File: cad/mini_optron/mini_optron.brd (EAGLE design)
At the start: 67 x 39.4 mm, 10 parts

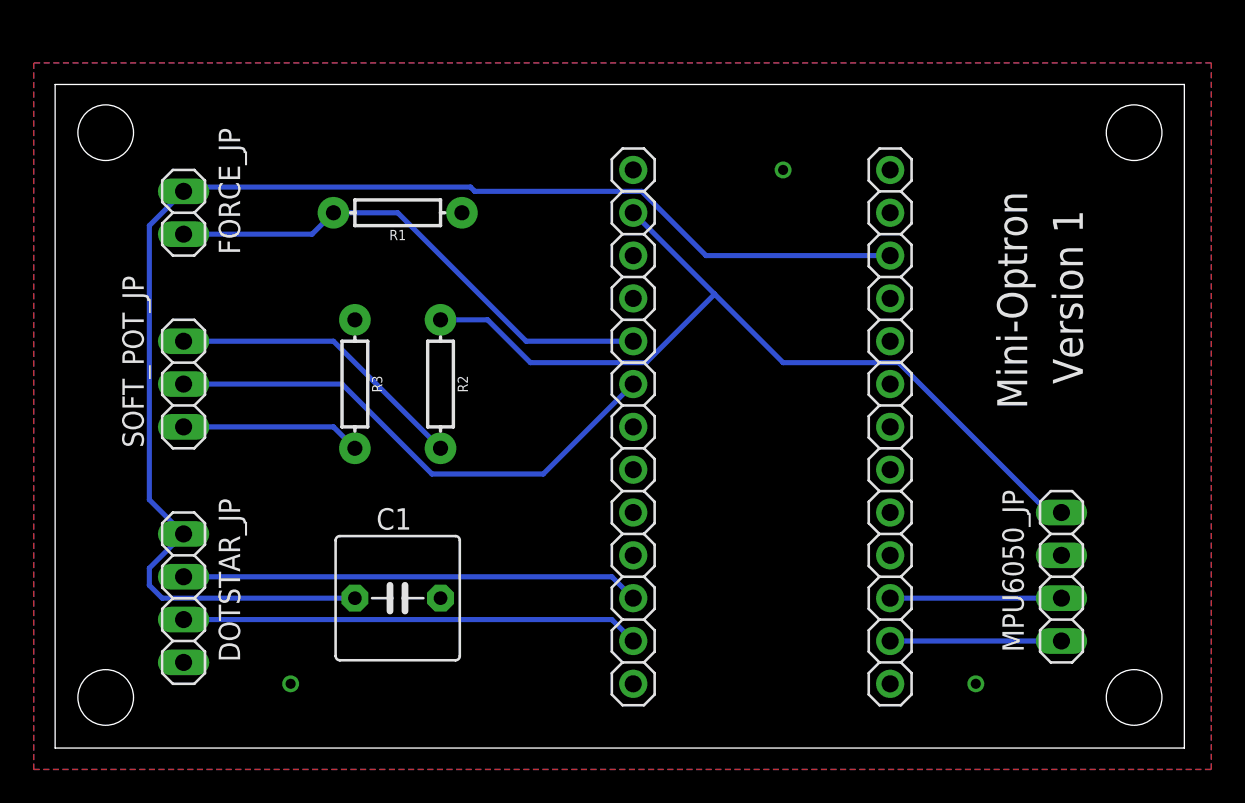
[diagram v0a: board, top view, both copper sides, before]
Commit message: Updated FSR circuit, c1 orient
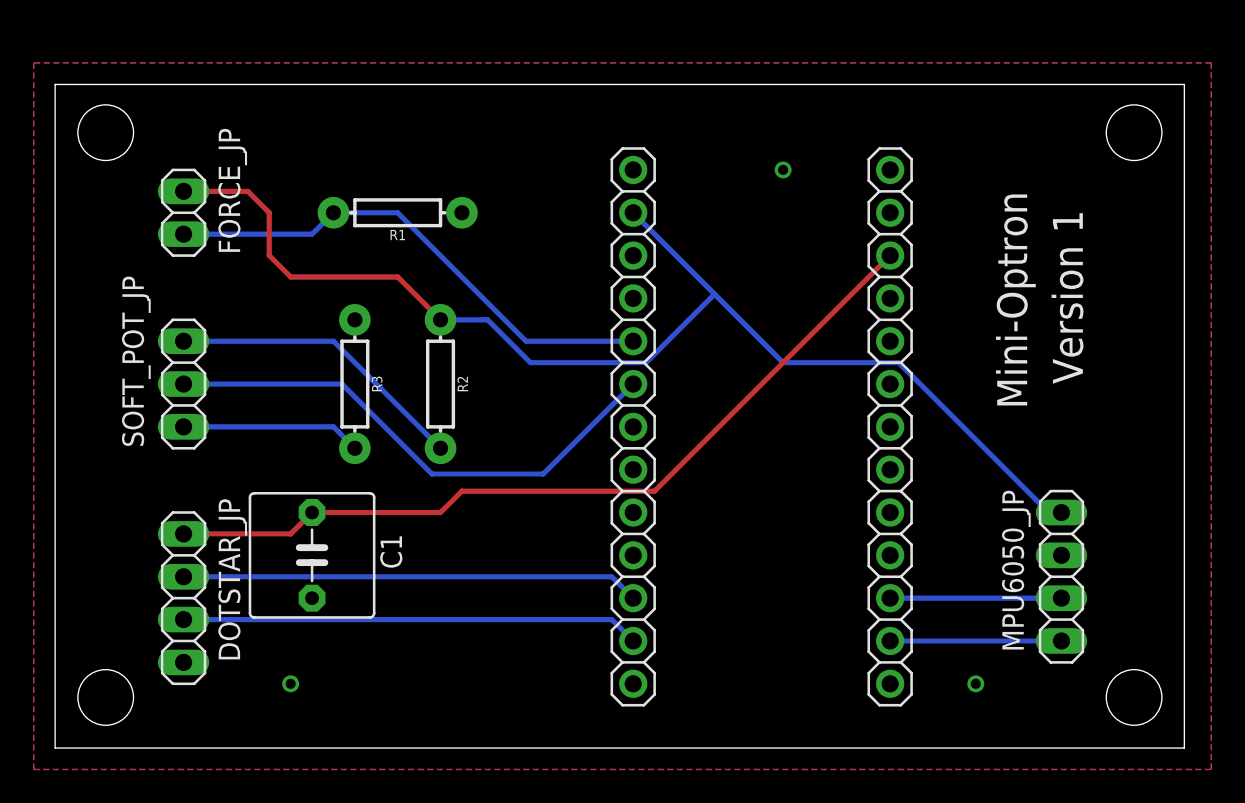
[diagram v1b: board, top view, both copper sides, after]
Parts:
- R1: value 2.2k -> 33k
- moved C1 5.68 mm to (15.2, 11.4), turned to 270 degrees
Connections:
- net CONN: now also FORCE_JP.1
- net VCC: no longer FORCE_JP.1
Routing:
- net VCC: track 82.1 -> 48.7 mm
- net CONN: track 51.8 -> 71.6 mm
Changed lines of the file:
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@@
 <?xml version="1.0" encoding="utf-8"?>
 <!DOCTYPE eagle SYSTEM "eagle.dtd">
-<eagle version="9.6.1">
+<eagle version="9.3.1">
 <drawing>
 <settings>
@@
 </autorouter>
 <elements>
-<element name="C1" library="capacitor-wima" library_urn="urn:adsk.eagle:library:116" package="C5B7.2" package3d_urn="urn:adsk.eagle:package:5430/1" value="1 uF" x="20.32" y="8.89" smashed="yes">
-<attribute name="MF" value="AVX" x="36.83" y="5.08" size="1.778" layer="27" display="off"/>
-<attribute name="MPN" value="0805YD105KAT2A" x="36.83" y="5.08" size="1.778" layer="27" display="off"/>
-<attribute name="NAME" x="19.05" y="12.954" size="1.27" layer="25" ratio="10"/>
-<attribute name="OC_NEWARK" value="95W9236" x="36.83" y="5.08" size="1.778" layer="27" display="off"/>
-<attribute name="POPULARITY" value="1" x="36.83" y="5.08" size="1.778" layer="27" display="off"/>
-<attribute name="VALUE" x="18.415" y="3.429" size="1.27" layer="27" ratio="10"/>
+<element name="C1" library="capacitor-wima" library_urn="urn:adsk.eagle:library:116" package="C5B7.2" package3d_urn="urn:adsk.eagle:package:5430/1" value="1 uF" x="15.24" y="11.43" smashed="yes" rot="R270">
+<attribute name="MF" value="AVX" x="11.43" y="-5.08" size="1.778" layer="27" rot="R270" display="off"/>
+<attribute name="MPN" value="0805YD105KAT2A" x="11.43" y="-5.08" size="1.778" layer="27" rot="R270" display="off"/>
+<attribute name="NAME" x="19.304" y="12.7" size="1.27" layer="25" ratio="10" rot="R270"/>
+<attribute name="OC_NEWARK" value="95W9236" x="11.43" y="-5.08" size="1.778" layer="27" rot="R270" display="off"/>
+<attribute name="POPULARITY" value="1" x="11.43" y="-5.08" size="1.778" layer="27" rot="R270" display="off"/>
+<attribute name="VALUE" x="9.779" y="13.335" size="1.27" layer="27" ratio="10" rot="R270"/>
 </element>
 <element name="DOTSTAR_JP" library="pinhead" library_urn="urn:adsk.eagle:library:325" package="1X04" package3d_urn="urn:adsk.eagle:package:22407/2" value="" x="7.62" y="8.89" smashed="yes" rot="R270">
@@
 <attribute name="VALUE" x="4.445" y="25.4" size="1.27" layer="27" rot="R270"/>
 </element>
-<element name="R1" library="SparkFun-Resistors" library_urn="urn:adsk.eagle:library:532" package="AXIAL-0.3" package3d_urn="urn:adsk.eagle:package:39658/1" value=" 2.2k" x="20.32" y="31.75" smashed="yes" rot="R180">
+<element name="R1" library="SparkFun-Resistors" library_urn="urn:adsk.eagle:library:532" package="AXIAL-0.3" package3d_urn="urn:adsk.eagle:package:39658/1" value="33k" x="20.32" y="31.75" smashed="yes" rot="R180">
 <attribute name="MF" value="VISHAY" x="20.32" y="31.75" size="1.778" layer="27" rot="R180" display="off"/>
 <attribute name="MPN" value="CRCW060310K0FKEA" x="20.32" y="31.75" size="1.778" layer="27" rot="R180" display="off"/>
@@
 <contactref element="C1" pad="1"/>
 <contactref element="DOTSTAR_JP" pad="1"/>
-<contactref element="FORCE_JP" pad="1"/>
-<wire x1="5.588" y1="10.668" x2="7.62" y2="12.7" width="0.3048" layer="16"/>
-<wire x1="5.588" y1="9.652" x2="5.588" y2="10.668" width="0.3048" layer="16"/>
-<wire x1="6.35" y1="8.89" x2="5.588" y2="9.652" width="0.3048" layer="16"/>
-<wire x1="17.78" y1="8.89" x2="6.35" y2="8.89" width="0.3048" layer="16"/>
-<wire x1="5.588" y1="30.988" x2="7.62" y2="33.02" width="0.3048" layer="16"/>
-<wire x1="5.588" y1="14.732" x2="5.588" y2="30.988" width="0.3048" layer="16"/>
-<wire x1="7.62" y1="12.7" x2="5.588" y2="14.732" width="0.3048" layer="16"/>
-<wire x1="38.608" y1="29.21" x2="49.53" y2="29.21" width="0.3048" layer="16"/>
-<wire x1="34.798" y1="33.02" x2="38.608" y2="29.21" width="0.3048" layer="16"/>
-<wire x1="24.892" y1="33.02" x2="34.798" y2="33.02" width="0.3048" layer="16"/>
-<wire x1="24.638" y1="33.274" x2="24.892" y2="33.02" width="0.3048" layer="16"/>
-<wire x1="7.874" y1="33.274" x2="24.638" y2="33.274" width="0.3048" layer="16"/>
-<wire x1="7.62" y1="33.02" x2="7.874" y2="33.274" width="0.3048" layer="16"/>
+<wire x1="49.53" y1="29.21" x2="35.56" y2="15.24" width="0.3048" layer="1"/>
+<wire x1="24.13" y1="15.24" x2="22.86" y2="13.97" width="0.3048" layer="1"/>
+<wire x1="22.86" y1="13.97" x2="15.24" y2="13.97" width="0.3048" layer="1"/>
+<wire x1="35.56" y1="15.24" x2="24.13" y2="15.24" width="0.3048" layer="1"/>
+<wire x1="15.24" y1="13.97" x2="13.97" y2="12.7" width="0.3048" layer="1"/>
+<wire x1="13.97" y1="12.7" x2="7.62" y2="12.7" width="0.3048" layer="1"/>
 </signal>
 <signal name="N$4">
@@
 <wire x1="35.052" y1="22.86" x2="28.194" y2="22.86" width="0.3048" layer="16"/>
 <wire x1="39.116" y1="26.924" x2="35.052" y2="22.86" width="0.3048" layer="16"/>
+<contactref element="FORCE_JP" pad="1"/>
+<wire x1="22.86" y1="25.4" x2="20.32" y2="27.94" width="0.3048" layer="1"/>
+<wire x1="13.97" y1="27.94" x2="12.7" y2="29.21" width="0.3048" layer="1"/>
+<wire x1="12.7" y1="29.21" x2="12.7" y2="31.75" width="0.3048" layer="1"/>
+<wire x1="12.7" y1="31.75" x2="11.43" y2="33.02" width="0.3048" layer="1"/>
+<wire x1="11.43" y1="33.02" x2="7.62" y2="33.02" width="0.3048" layer="1"/>
+<wire x1="20.32" y1="27.94" x2="13.97" y2="27.94" width="0.3048" layer="1"/>
 </signal>
 <signal name="N$2">

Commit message: Add files via upload
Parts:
- removed R2: 10k, SparkFun-Resistors:AXIAL-0.3
- R1: value 33k -> 10K
- moved MPU6050_JP 51.1 mm to (8.62, 11.9)
- moved DOTSTAR_JP 39.8 mm to (39.1, 33.2)
- moved C1 27.4 mm to (31.5, 33.5), turned to 90 degrees
- moved JP2 14.6 mm to (41.6, 6.81), turned to 180 degrees
- moved JP1 7.94 mm to (41.6, 22.1), turned to 180 degrees
- moved R1 4.11 mm to (17.5, 34.8)
- moved FORCE_JP 3.16 mm to (8.62, 34.8)
- moved SOFT_POT_JP 3.16 mm to (8.62, 24.6)
- moved R3 1.75 mm to (17.5, 23.3), turned to 180 degrees
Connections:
- net N$1 renamed A0
- removed net CONN: FORCE_JP.1, JP1.2, MPU6050_JP.1, R2.P$1
- removed net N$10: JP2.12, MPU6050_JP.4
- removed net N$2: DOTSTAR_JP.2, JP1.11
- removed net N$3: R2.P$2, SOFT_POT_JP.1
- removed net N$4: JP1.6, SOFT_POT_JP.2
- removed net N$5: R3.P$2, SOFT_POT_JP.3
- removed net N$6: DOTSTAR_JP.3, JP1.12
- removed net N$9: JP2.11, MPU6050_JP.3
- removed net VCC: C1.1, DOTSTAR_JP.1, JP2.3
- new net 3V: FORCE_JP.1, JP1.2, MPU6050_JP.3, SOFT_POT_JP.1
- new net 5V: C1.1, DOTSTAR_JP.3, JP2.3
- new net A1: JP1.6, R3.P$2, SOFT_POT_JP.3
- new net MOSI: DOTSTAR_JP.2, JP1.12
- new net SCK: DOTSTAR_JP.1, JP1.11
- new net SCL: JP2.11, MPU6050_JP.1
- new net SDA: JP2.12, MPU6050_JP.2
- net GND: now also MPU6050_JP.4, SOFT_POT_JP.2; no longer MPU6050_JP.2
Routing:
- net 3V: track 0.00 -> 79.1 mm
- net CONN: track 71.6 -> 0.00 mm
- net SCK: track 0.00 -> 54.2 mm
- net 5V: track 0.00 -> 52.4 mm
- net VCC: track 48.7 -> 0.00 mm
- net A1: track 0.00 -> 38.2 mm
- net N$4: track 31.1 -> 0.00 mm
- net N$6: track 27.2 -> 0.00 mm
- net N$2: track 27.2 -> 0.00 mm
- net SCL: track 0.00 -> 26.5 mm
- net SDA: track 0.00 -> 23.0 mm
- net MOSI: track 0.00 -> 20.4 mm
- net N$3: track 17.9 -> 0.00 mm
- net A0: track 30.4 -> 43.9 mm
- net N$5: track 10.7 -> 0.00 mm
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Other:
- board size 67 x 39.4 mm -> 65.2 x 41.1 mm
- board text added: "Mini-Optron Version 2"
- board text removed: "Mini-Optron"
- board text removed: "Version 1"
